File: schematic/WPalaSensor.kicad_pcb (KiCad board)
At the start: 2 copper layers, 25.4 x 29.8 mm, 8 parts, among them P3 Palazzetti Connector, U1 WeMos_mini, U3 DS18B20, U4 MCP4151-50k, U5 MCP4151-5k

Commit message: Update schematic
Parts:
- removed P3: Palazzetti Connector, Connect:bornier2
- removed U3: DS18B20, Pin_Headers:Pin_Header_Straight_1x03_Pitch2.54mm
- removed U4: MCP4151-50k, Housings_DIP:DIP-8_W7.62mm_LongPads
- removed U5: MCP4151-5k, Housings_DIP:DIP-8_W7.62mm_LongPads
- added C1: 100n, Capacitor_SMD:C_0805_2012Metric_Pad1.18x1.45mm_HandSolder, F.Cu at (41.4, 29.6)
- added C2: 10u, Capacitor_Tantalum_SMD:CP_EIA-3216-18_Kemet-A_Pad1.58x1.35mm_HandSolder, F.Cu at (43.9, 30.2)
- added J1: WeMos_mini_Hat_Left, wemos_d1_mini:WeMos_D1_mini_Hat_Left, B.Cu at (25.4, 25.4)
- added J2: WeMos_mini_Hat_Right, wemos_d1_mini:WeMos_D1_mini_Hat_Right, B.Cu at (48.3, 25.4)
- added J3: Fumis T01, TerminalBlock:TerminalBlock_bornier-2_P5.08mm, F.Cu at (34.3, 21.6)
- added R3: 4.7K, Resistor_SMD:R_0805_2012Metric_Pad1.20x1.40mm_HandSolder, F.Cu at (31.1, 32.4)
- added R4: 2.2K 1%, Resistor_SMD:R_0805_2012Metric_Pad1.20x1.40mm_HandSolder, F.Cu at (36.8, 28.6)
- added U2: MCP4725, Package_TO_SOT_SMD:SOT-23-6_Handsoldering, F.Cu at (36.8, 33.0)
- C3: value 1uF -> 100n; footprint Capacitors_SMD:C_0805_HandSoldering -> Capacitor_SMD:C_0805_2012Metric_Pad1.18x1.45mm_HandSolder; moved to F.Cu
- R1, R2: footprint Resistors_SMD:R_0805_HandSoldering -> Resistor_SMD:R_0805_2012Metric_Pad1.20x1.40mm_HandSolder; moved to F.Cu
- U1: value WeMos_mini -> DS18B20; footprint wemos_d1_mini:wemos-d1-mini-DIL-only -> Connector_PinHeader_2.54mm:PinHeader_1x03_P2.54mm_Vertical; moved to F.Cu
- moved R2 15.3 mm to (31.1, 28.6), turned to 180 degrees
- moved C3 9.88 mm to (42.7, 34.5), turned to 0 degrees
- moved R1 9.04 mm to (42.7, 39.4), turned to 180 degrees
- moved U1 2.29 mm to (31.1, 40.0)
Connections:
- C3 pad 1: VCC -> Net-(U2-VOUT)
- C3 pad 2: Net-(C3-Pad2) -> GND
- R1 pad 2: Net-(R1-Pad2) -> Net-(J1-D4)
- R2 pad 1: Net-(R2-Pad1) -> VCC
- R2 pad 2: Net-(R2-Pad2) -> Net-(J1-D1)
- U1 pad 1: (no net) -> GND
- U1 pad 2: GND -> Net-(J1-D4)
- U1 pad 3: Net-(R1-Pad2) -> VCC
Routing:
- net Net-(R2-Pad1): track 36.4 -> 0.00 mm
- net Net-(U1-Pad12): track 32.4 -> 0.00 mm
- net Net-(R1-Pad2): track 23.6 -> 0.00 mm
- net GND: track 19.8 -> 41.4 mm
- net Net-(C3-Pad2): track 19.0 -> 0.00 mm
- net Net-(J1-D4): track 0.00 -> 17.8 mm
- net Net-(J1-D1): track 0.00 -> 17.7 mm
- net Net-(U4-Pad6): track 15.1 -> 0.00 mm
- net Net-(J1-D2): track 0.00 -> 12.6 mm, vias 0 -> 1
- net Net-(U1-Pad6): track 11.7 -> 0.00 mm
- net Net-(U1-Pad5): track 10.4 -> 0.00 mm
- net Net-(U2-VOUT): track 0.00 -> 10.3 mm
- net Net-(J3-Pin_2): track 0.00 -> 8.45 mm
- net Net-(R2-Pad2): track 3.17 -> 0.00 mm
- net VCC: track 61.9 -> 62.4 mm
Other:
- board size 25.4 x 29.8 mm -> 25.4 x 27 mm
- board text added: "C1,C3: 100n C2: 10u R1,R2,R3: 4.7K R4: 2.2K 1% U2: MCP4725"
- board text added: "JLCJLCJLCJLC"
- board text added: "V3.0"
- board text added: "WPalaSensor"
- board text removed: "50k"
- board text removed: "5k"
- board text removed: "D5"
- board text removed: "D6"
- board text removed: "D7"
- board text removed: "PALA"
- board text removed: "V2.0"
- board text removed: "WirelessPalaSensor"

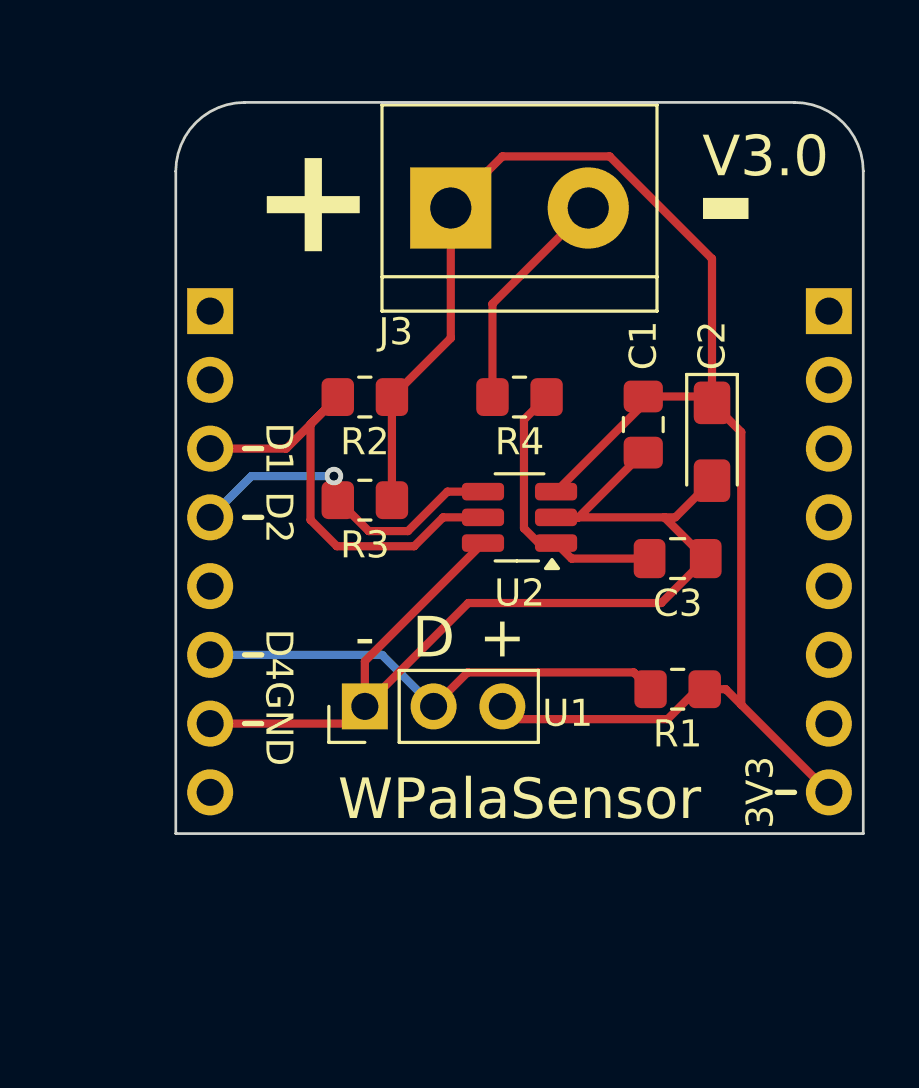
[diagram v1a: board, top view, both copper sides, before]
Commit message: Update PCB according to new schematic
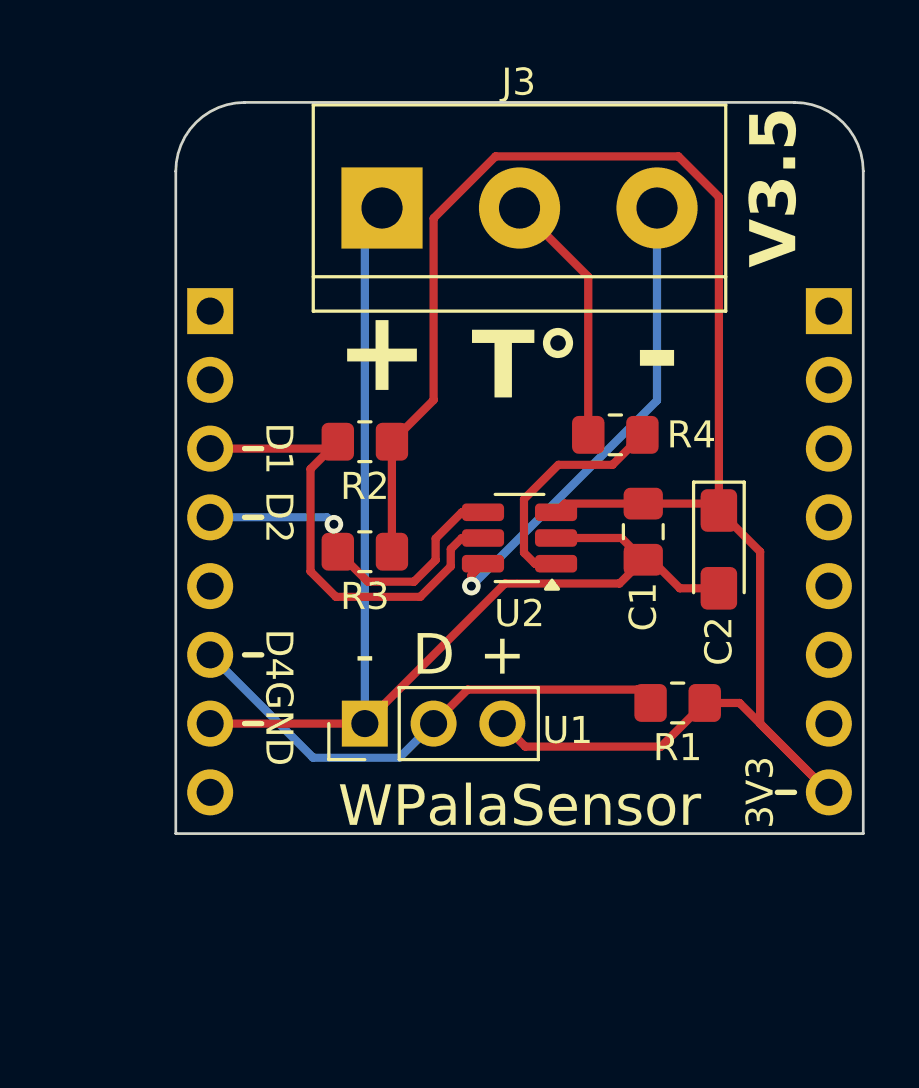
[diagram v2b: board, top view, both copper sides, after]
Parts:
- removed C3: 100n, Capacitor_SMD:C_0805_2012Metric_Pad1.18x1.45mm_HandSolder
- J3: footprint TerminalBlock:TerminalBlock_bornier-2_P5.08mm -> TerminalBlock:TerminalBlock_bornier-3_P5.08mm
- U2: value MCP4725 -> MCP4726
- moved C2 3.99 mm to (44.2, 34.2)
- moved C1 3.96 mm to (41.4, 33.5)
- moved R4 3.81 mm to (40.4, 30.0)
- moved J3 2.54 mm to (31.8, 21.6)
- moved R3 1.91 mm to (31.1, 34.3)
- moved R2 1.65 mm to (31.1, 30.2)
- moved U2 0.76 mm to (36.8, 33.8)
- moved U1 0.63 mm to (31.1, 40.6)
- moved R1 0.51 mm to (42.7, 39.9)
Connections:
- J3 pad 1: VCC -> GND
- U2 pad 6: GND -> Net-(J3-Pin_3)
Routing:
- net Net-(J3-Pin_3): track 0.00 -> 17.8 mm, vias 0 -> 1
- net VCC: track 62.4 -> 69.5 mm
- net GND: track 41.4 -> 44.6 mm
- net Net-(U2-VOUT): track 10.3 -> 8.69 mm
- net Net-(J1-D4): track 17.8 -> 19.1 mm
- net Net-(J3-Pin_2): track 8.45 -> 9.43 mm
- net Net-(J1-D2): track 12.6 -> 13.1 mm
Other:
- board text added: "C1: 100n C2: 10u R1,R2,R3: 4.7K R4: 2.2K 1% U2: MCP4726"
- board text added: "T°"
- board text added: "V3.5"
- board text removed: "C1,C3: 100n C2: 10u R1,R2,R3: 4.7K R4: 2.2K 1% U2: MCP4725"
- board text removed: "V3.0"
